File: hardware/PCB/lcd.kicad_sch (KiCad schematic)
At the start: 72 parts, among them U1 TSC2013QRSARQ1, U2 TPS923650

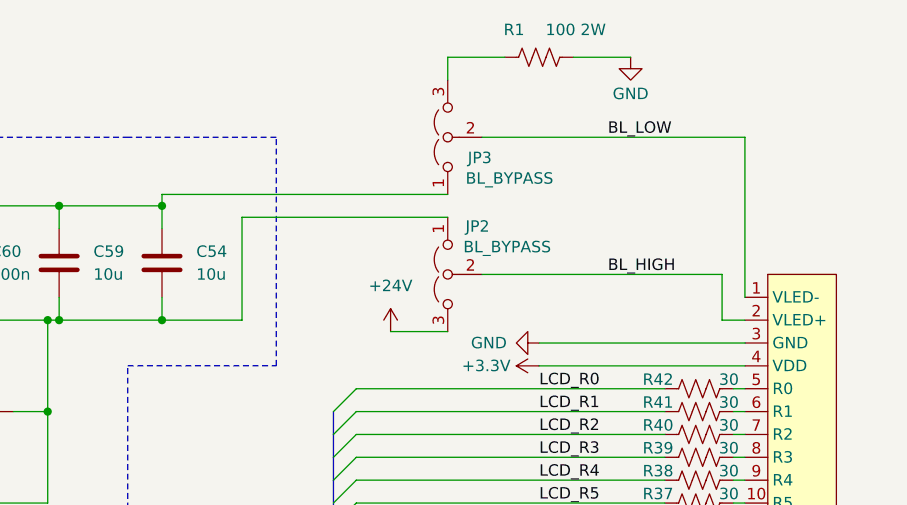
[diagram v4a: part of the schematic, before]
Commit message: Add more symbols and continue filling footprints
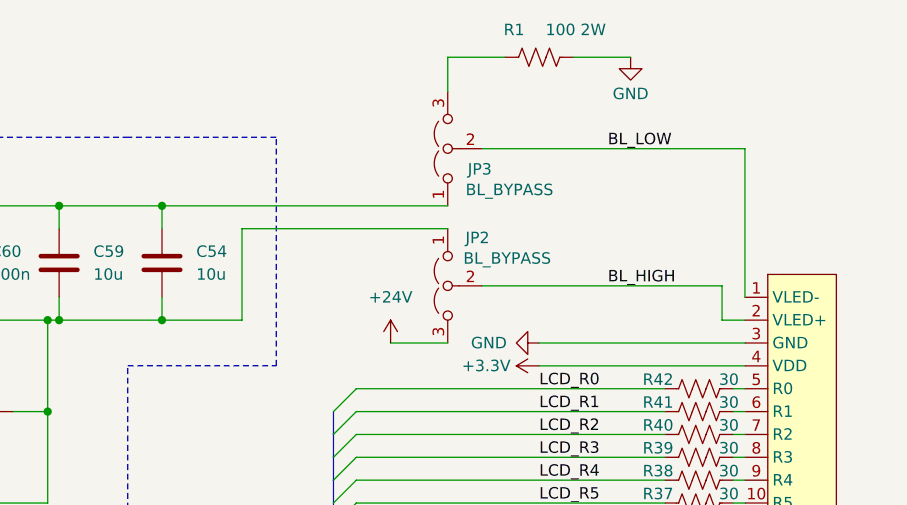
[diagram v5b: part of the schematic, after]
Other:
- moved on the sheet: JP2, JP3
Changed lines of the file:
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@@
 	(wire
 		(pts
-			(xy 193.04 26.67) (xy 193.04 29.21)
+			(xy 193.04 26.67) (xy 193.04 30.48)
 		)
 		(stroke
@@
 	(wire
 		(pts
-			(xy 161.29 41.91) (xy 161.29 43.18)
-		)
-		(stroke
-			(width 0)
-			(type default)
-		)
-	)
-	(wire
-		(pts
 			(xy 224.79 86.36) (xy 226.06 86.36)
 		)
@@
 	(wire
 		(pts
-			(xy 161.29 41.91) (xy 193.04 41.91)
+			(xy 161.29 43.18) (xy 193.04 43.18)
 		)
 		(stroke
@@
 	(wire
 		(pts
-			(xy 226.06 35.56) (xy 226.06 53.34)
+			(xy 226.06 36.83) (xy 226.06 53.34)
 		)
 		(stroke
@@
 	(wire
 		(pts
-			(xy 196.85 35.56) (xy 226.06 35.56)
+			(xy 196.85 36.83) (xy 226.06 36.83)
 		)
 		(stroke
@@
 	(wire
 		(pts
-			(xy 170.18 44.45) (xy 193.04 44.45)
+			(xy 170.18 45.72) (xy 193.04 45.72)
 		)
 		(stroke
@@
 	(wire
 		(pts
-			(xy 199.39 26.67) (xy 193.04 26.67)
+			(xy 193.04 26.67) (xy 199.39 26.67)
 		)
 		(stroke
@@
 	(wire
 		(pts
-			(xy 186.69 57.15) (xy 193.04 57.15)
+			(xy 186.69 58.42) (xy 193.04 58.42)
 		)
 		(stroke
@@
 	(wire
 		(pts
-			(xy 170.18 44.45) (xy 170.18 55.88)
+			(xy 170.18 45.72) (xy 170.18 55.88)
 		)
 		(stroke
@@
 	(wire
 		(pts
-			(xy 223.52 55.88) (xy 223.52 50.8)
+			(xy 223.52 55.88) (xy 223.52 52.07)
 		)
 		(stroke
@@
 	(wire
 		(pts
-			(xy 196.85 50.8) (xy 223.52 50.8)
+			(xy 196.85 52.07) (xy 223.52 52.07)
 		)
 		(stroke
@@
 	)
 	(label "BL_LOW"
-		(at 210.82 35.56 0)
+		(at 210.82 36.83 0)
 		(effects
 			(font
@@
 	)
 	(label "BL_HIGH"
-		(at 210.82 50.8 0)
+		(at 210.82 52.07 0)
 		(effects
 			(font
@@
 	(symbol
 		(lib_id "Jumper:Jumper_3_Open")
-		(at 193.04 50.8 90)
+		(at 193.04 52.07 90)
 		(mirror x)
 		(unit 1)
@@
 		(dnp no)
 		(property "Reference" "JP2"
-			(at 196.342 45.466 90)
+			(at 196.342 46.736 90)
 			(effects
 				(font
@@
 		)
 		(property "Value" "BL_BYPASS"
-			(at 199.644 47.752 90)
+			(at 199.644 49.022 90)
 			(effects
 				(font
@@
 		)
 		(property "Footprint" "Connector_PinHeader_2.54mm:PinHeader_1x03_P2.54mm_Vertical"
-			(at 193.04 50.8 0)
+			(at 193.04 52.07 0)
 			(effects
 				(font
@@
 		)
 		(property "Datasheet" "~"
-			(at 193.04 50.8 0)
+			(at 193.04 52.07 0)
 			(effects
 				(font
@@
 		)
 		(property "Description" "Jumper, 3-pole, both open"
-			(at 193.04 50.8 0)
+			(at 193.04 52.07 0)
 			(effects
 				(font
@@
 		)
 		(property "Manufacturer_Part_Number" ""
-			(at 193.04 50.8 0)
+			(at 193.04 52.07 0)
 			(effects
 				(font
@@
 	(symbol
 		(lib_id "Jumper:Jumper_3_Open")
-		(at 193.04 35.56 90)
+		(at 193.04 36.83 90)
 		(unit 1)
 		(exclude_from_sim no)
@@
 		(dnp no)
 		(property "Reference" "JP3"
-			(at 196.596 37.846 90)
+			(at 196.596 39.116 90)
 			(effects
 				(font
@@
 		)
 		(property "Value" "BL_BYPASS"
-			(at 199.898 40.132 90)
+			(at 199.898 41.402 90)
 			(effects
 				(font
@@
 		)
 		(property "Footprint" "Connector_PinHeader_2.54mm:PinHeader_1x03_P2.54mm_Vertical"
-			(at 193.04 35.56 0)
+			(at 193.04 36.83 0)
 			(effects
 				(font
@@
 		)
 		(property "Datasheet" "~"
-			(at 193.04 35.56 0)
+			(at 193.04 36.83 0)
 			(effects
 				(font
@@
 		)
 		(property "Description" "Jumper, 3-pole, both open"
-			(at 193.04 35.56 0)
+			(at 193.04 36.83 0)
 			(effects
 				(font
@@
 		)
 		(property "Manufacturer_Part_Number" ""
-			(at 193.04 35.56 0)
+			(at 193.04 36.83 0)
 			(effects
 				(font
@@
 	(symbol
 		(lib_id "power:+24V")
-		(at 186.69 57.15 0)
+		(at 186.69 58.42 0)
 		(unit 1)
 		(exclude_from_sim no)
@@
 		(fields_autoplaced yes)
 		(property "Reference" "#PWR045"
-			(at 186.69 60.96 0)
+			(at 186.69 62.23 0)
 			(effects
 				(font
@@
 		)
 		(property "Value" "+24V"
-			(at 186.69 52.07 0)
+			(at 186.69 53.34 0)
 			(effects
 				(font
@@
 		)
 		(property "Footprint" ""
-			(at 186.69 57.15 0)
+			(at 186.69 58.42 0)
 			(effects
 				(font
@@
 		)
 		(property "Datasheet" ""
-			(at 186.69 57.15 0)
+			(at 186.69 58.42 0)
 			(effects
 				(font
@@
 		)
 		(property "Description" "Power symbol creates a global label with name \"+24V\""
-			(at 186.69 57.15 0)
+			(at 186.69 58.42 0)
 			(effects
 				(font

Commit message: Finished setting footprints for LCD, motors, RPi, and storage schematics
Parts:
- JP2, JP3: now in the parts list
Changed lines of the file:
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@@
 		(unit 1)
 		(exclude_from_sim no)
-		(in_bom no)
+		(in_bom yes)
 		(on_board yes)
 		(dnp no)
@@
 		(unit 1)
 		(exclude_from_sim no)
-		(in_bom no)
-		(on_board yes)
-		(dnp no)
+		(in_bom yes)
+		(on_board yes)
+		(dnp no)

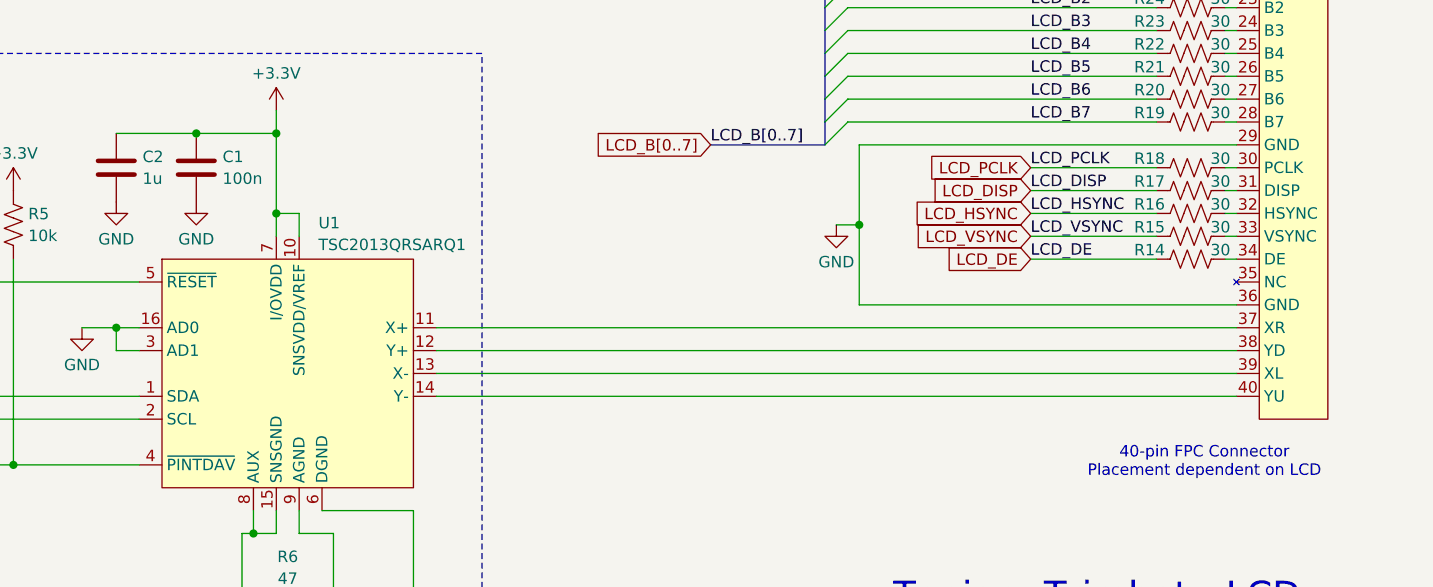
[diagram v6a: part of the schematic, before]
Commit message: Touch up some ERC violations
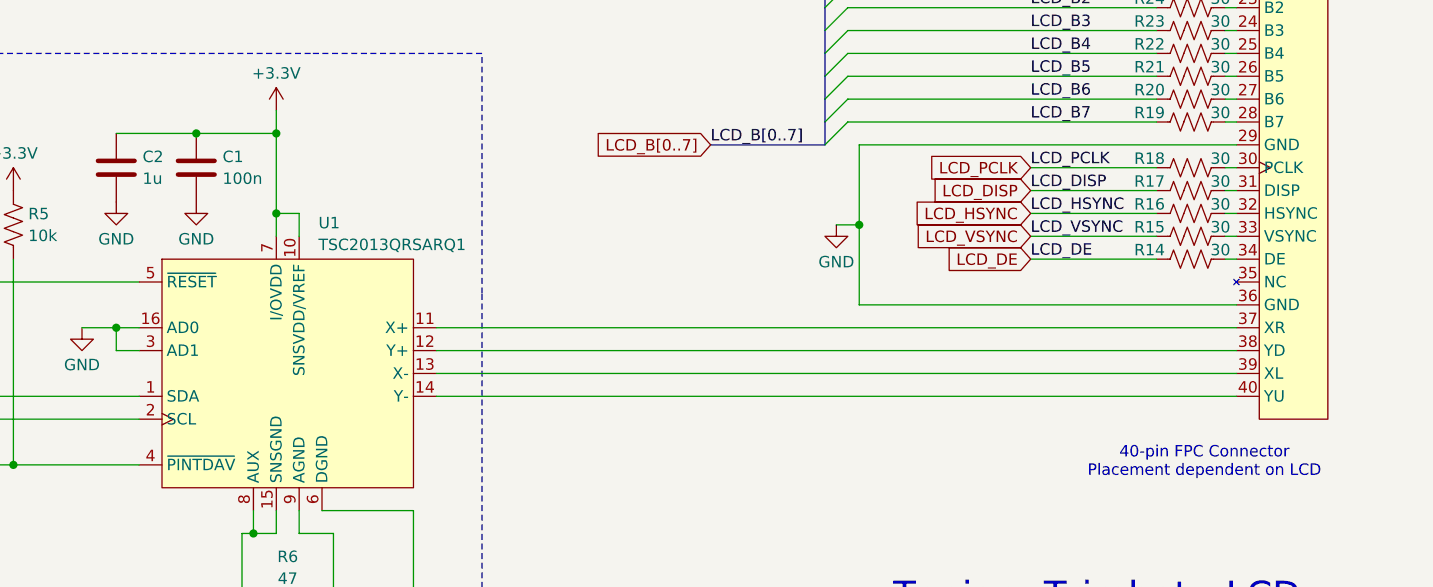
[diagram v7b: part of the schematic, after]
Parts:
- U2: footprint Package_SO:Texas_DGN0008B_VSSOP-8-1EP_3x3mm_P0.65mm_EP2x3mm_Mask1.88x1.98mm -> Package_SO:HVSSOP-8-1EP_3x3mm_P0.65mm_EP1.57x1.89mm
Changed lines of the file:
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@@
 		(on_board yes)
 		(dnp no)
-		(property "Reference" "#PWR044"
+		(property "Reference" "#PWR0157"
 			(at 29.21 62.23 0)
 			(effects
@@
 			(project "TopiaryTrimbot"
 				(path "/2826ff7c-9767-4078-8ea2-1cd3a432abf3/e982bc10-c57a-42ac-b92d-a536dd69a0fd"
-					(reference "#PWR044")
+					(reference "#PWR0157")
 					(unit 1)
 				)
@@
 			)
 		)
-		(property "Footprint" "Package_SO:Texas_DGN0008B_VSSOP-8-1EP_3x3mm_P0.65mm_EP2x3mm_Mask1.88x1.98mm"
+		(property "Footprint" "Package_SO:HVSSOP-8-1EP_3x3mm_P0.65mm_EP1.57x1.89mm"
 			(at 65.278 94.742 0)
 			(effects
@@
 			)
 		)
-		(property "Datasheet" "https://www.ti.com/lit/ds/symlink/tps923650.pdf?ts=1770010181159&ref_url=https%253A%252F%252Fwww.ti.com%252Fproduct%252FTPS923650"
+		(property "Datasheet" "https://www.ti.com/lit/ds/symlink/tps923650.pdf?ts=1770433717174&ref_url=https%253A%252F%252Fwww.ti.com%252Fproduct%252FTPS923650"
 			(at 70.358 94.996 0)
 			(effects
@@
 			)
 		)
-		(property "Description" "65V 1A Boost/Buck-Boost LED Driver with PWM/Analog Dimming"
+		(property "Description" "65V 1A Boost/Buck-Boost LED Driver with PWM Dimming"
 			(at 67.31 94.996 0)
 			(effects
@@
 		(on_board yes)
 		(dnp no)
-		(property "Reference" "#PWR043"
+		(property "Reference" "#PWR0158"
 			(at 29.21 77.47 0)
 			(effects
@@
 			(project "TopiaryTrimbot"
 				(path "/2826ff7c-9767-4078-8ea2-1cd3a432abf3/e982bc10-c57a-42ac-b92d-a536dd69a0fd"
-					(reference "#PWR043")
+					(reference "#PWR0158")
 					(unit 1)
 				)
@@
 			)
 		)
-		(property "Datasheet" "https://www.hirose.com/product/document?clcode=&productname=&series=FH12&documenttype=Catalog&lang=en&documentid=D31648_en"
+		(property "Datasheet" "https://cdn-shop.adafruit.com/product-files/1591/CH430WQ12A-T+display+diagram.png"
 			(at 231.902 160.02 0)
 			(effects
@@
 			)
 		)
-		(property "Description" ""
+		(property "Description" "4.3\" TFT 480x272 RGB with Resistive Touchscreen"
 			(at 228.6 104.14 0)
 			(effects
@@
 		(on_board yes)
 		(dnp no)
-		(property "Reference" "#PWR046"
+		(property "Reference" "#PWR0159"
 			(at 213.36 33.02 0)
 			(effects
@@
 			(project "TopiaryTrimbot"
 				(path "/2826ff7c-9767-4078-8ea2-1cd3a432abf3/e982bc10-c57a-42ac-b92d-a536dd69a0fd"
-					(reference "#PWR046")
+					(reference "#PWR0159")
 					(unit 1)
 				)
@@
 		(dnp no)
 		(fields_autoplaced yes)
-		(property "Reference" "#PWR045"
+		(property "Reference" "#PWR0160"
 			(at 186.69 62.23 0)
 			(effects
@@
 			(project "TopiaryTrimbot"
 				(path "/2826ff7c-9767-4078-8ea2-1cd3a432abf3/e982bc10-c57a-42ac-b92d-a536dd69a0fd"
-					(reference "#PWR045")
+					(reference "#PWR0160")
 					(unit 1)
 				)

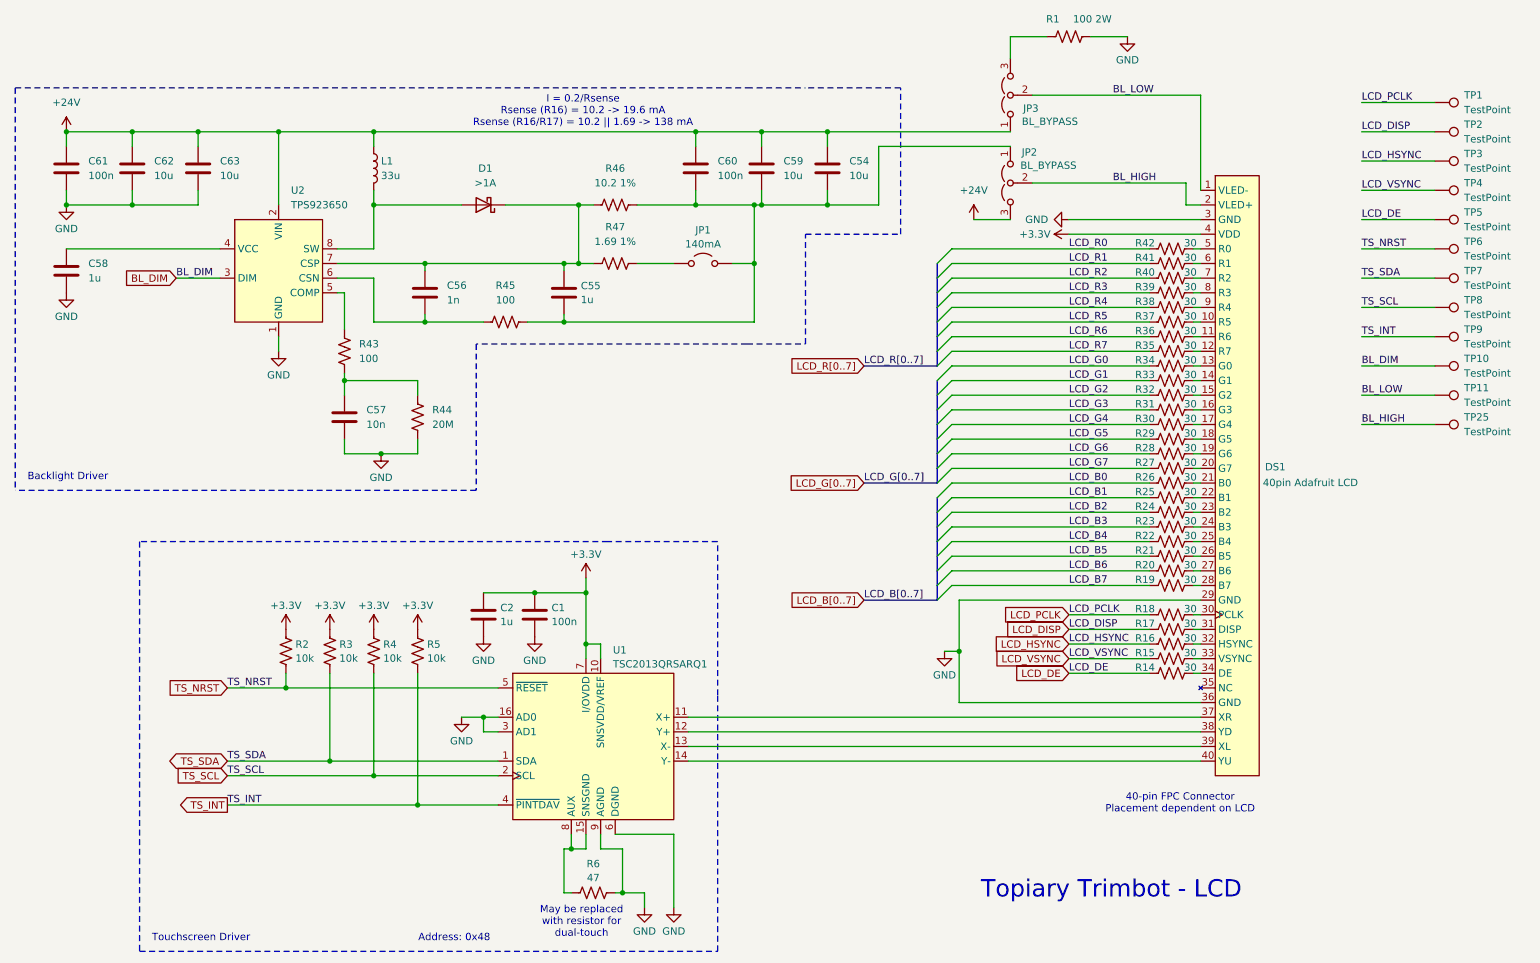
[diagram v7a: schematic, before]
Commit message: Synchronized schematic draft and reannotated all
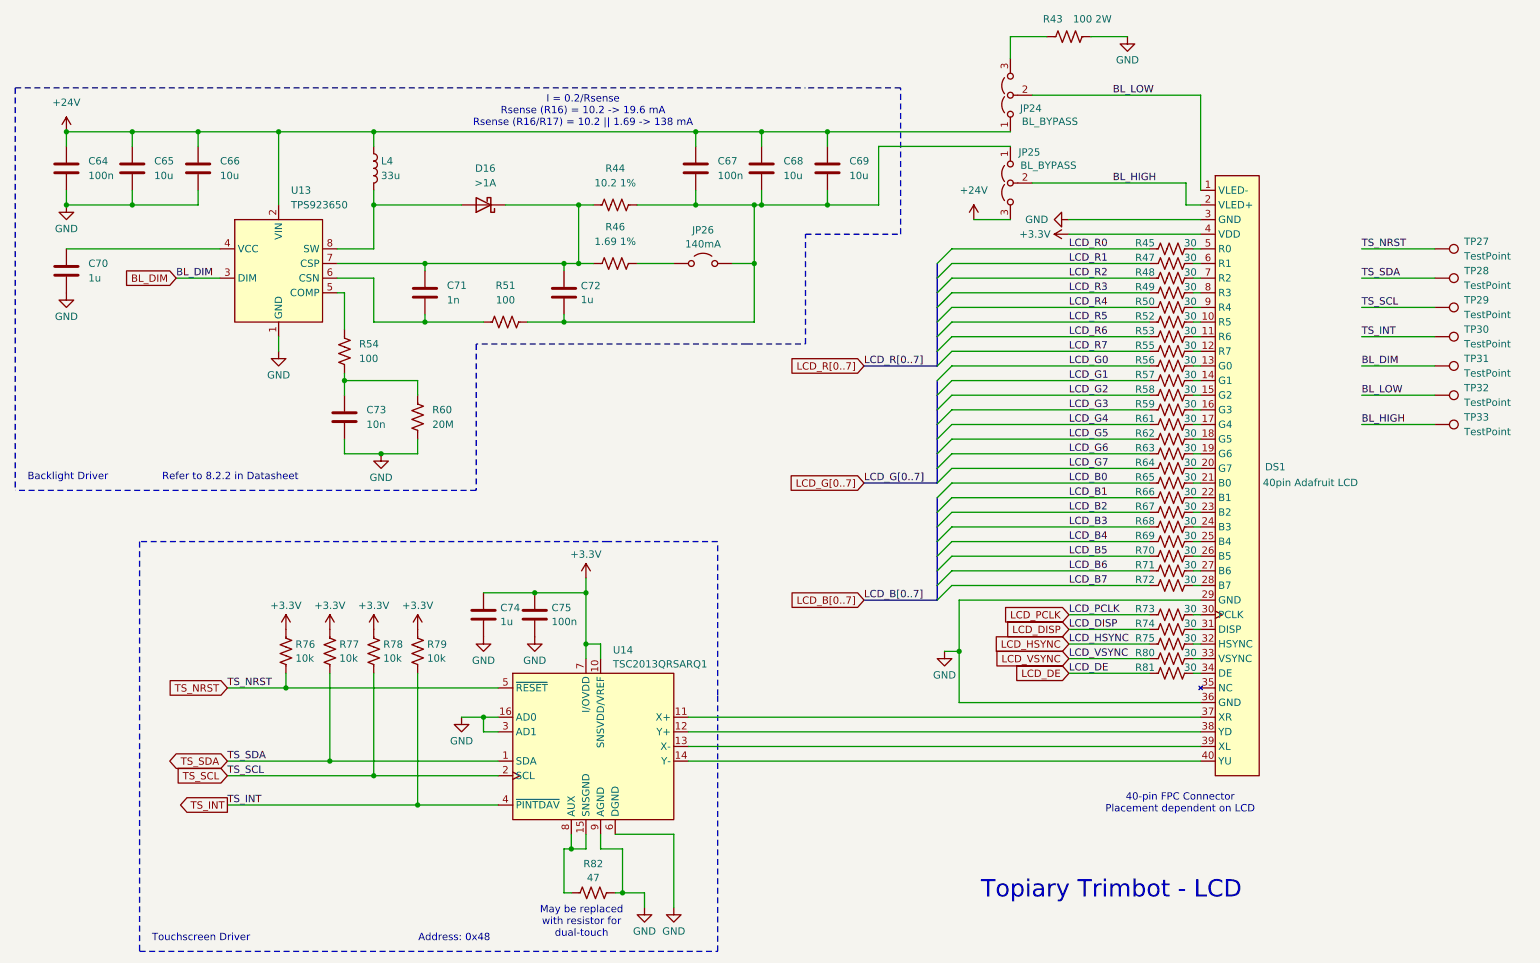
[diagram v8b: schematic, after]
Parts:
- removed TP1, TP2, TP3, TP4, TP5: TestPoint, TestPoint:TestPoint_Pad_D1.5mm, symbol Connector:TestPoint
- renumbered C61 to C64, C62 to C65, C63 to C66, C60 to C67, C59 to C68, C54 to C69, C58 to C70, C56 to C71, C55 to C72, C57 to C73, C2 to C74, C1 to C75, D1 to D16, JP3 to JP24, JP2 to JP25, JP1 to JP26, L1 to L4, R1 to R43, R46 to R44, R42 to R45, R47 to R46, R41 to R47, R40 to R48, R39 to R49, R38 to R50, R45 to R51, R37 to R52, R36 to R53, R43 to R54, R35 to R55, R34 to R56, R33 to R57, R32 to R58, R31 to R59, R44 to R60, R30 to R61, R29 to R62, R28 to R63, R27 to R64, R26 to R65, R25 to R66, R24 to R67, R23 to R68, R22 to R69, R21 to R70, R20 to R71, R19 to R72, R18 to R73, R17 to R74, R16 to R75, R2 to R76, R3 to R77, R4 to R78, R5 to R79, R15 to R80, R14 to R81, R6 to R82, TP6 to TP27, TP7 to TP28, TP8 to TP29, TP9 to TP30, TP10 to TP31, TP11 to TP32, TP25 to TP33, U2 to U13, U1 to U14
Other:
- note added: "Refer to 8.2.2 in Datasheet"
